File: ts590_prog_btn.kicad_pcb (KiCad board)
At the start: 2 copper layers, 80 x 50 mm, 23 parts, among them J1 DB9, J2 JACK_TRS_6PINS, J3 RJ45, P1 CONN_02X04, SW1 PTT, SW2 PF2, SW3 PF4, SW4 PF1, SW5 PF3, SW6 UP, SW7 DOWN, SW9 PTT_LOCK

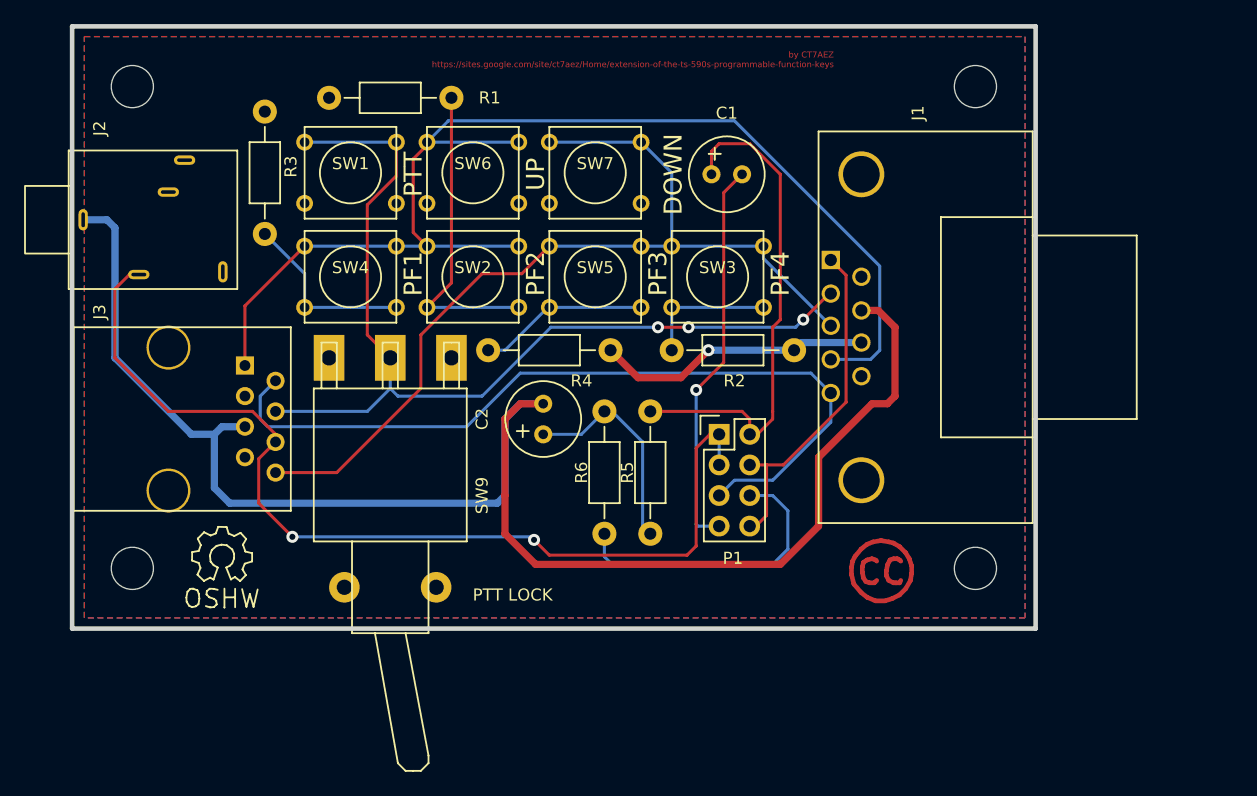
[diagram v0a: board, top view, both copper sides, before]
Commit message: Corrected DB-9 position on PCB
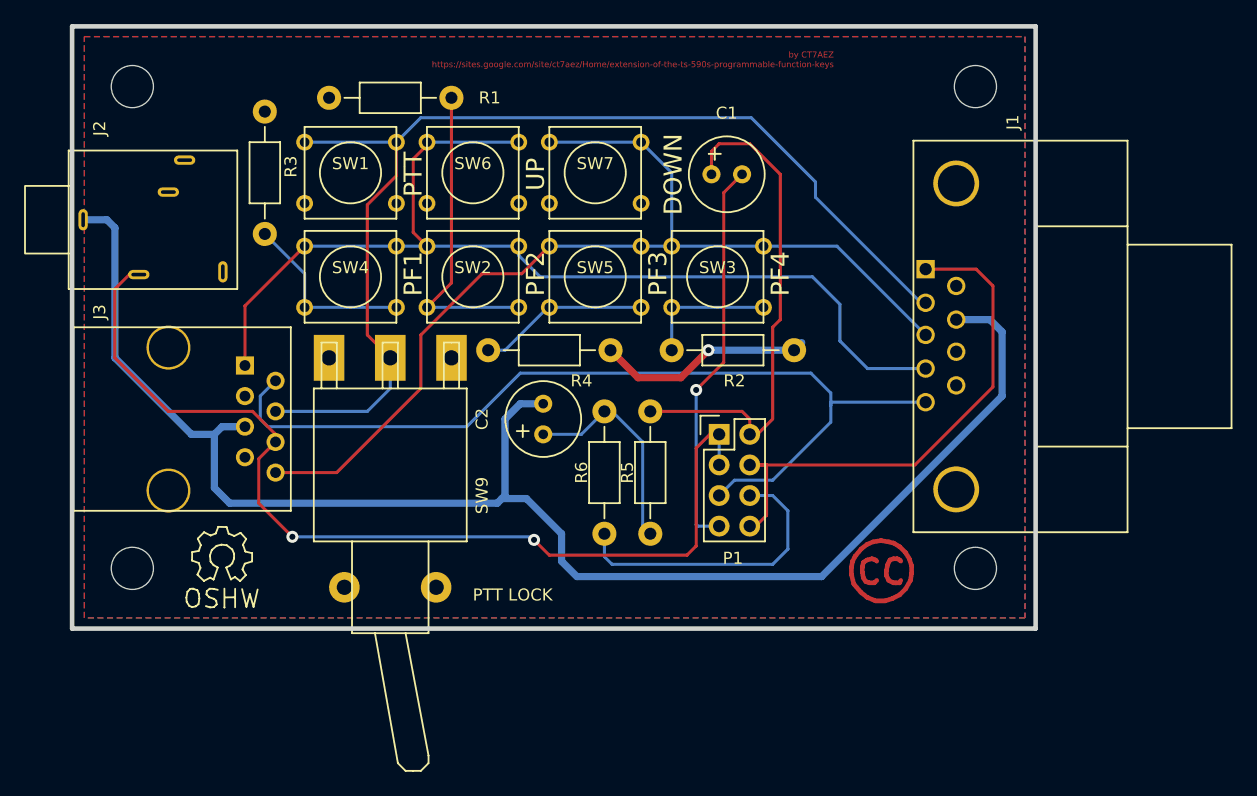
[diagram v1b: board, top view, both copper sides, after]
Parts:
- moved J1 7.91 mm to (181.6, 74.9)
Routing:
- net /MICCN1_MIC: track 28.5 -> 44.8 mm
- net /MICCN4_UP: track 101.6 -> 87.2 mm
- net /MICCN2_PTT: track 80.5 -> 92.1 mm, vias 3 -> 0
- net /MICCN5_8V: track 68.1 -> 76.2 mm
- net /MICCN3_DOWN: track 77.1 -> 84.7 mm
- net GND: track 23.0 -> 18.0 mm
- net GNDA: track 131.7 -> 128.1 mm
